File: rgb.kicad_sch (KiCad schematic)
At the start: 55 parts, among them Q1 BSS138, Q2 BSS138, U3 NSI50350ADT4G

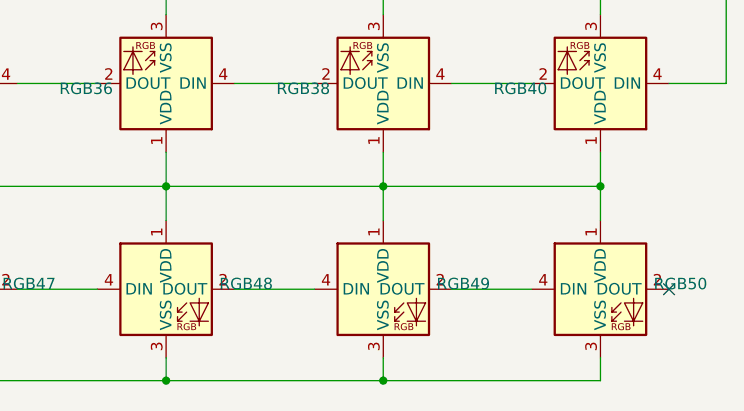
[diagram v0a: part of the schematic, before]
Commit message: finished pcb routing
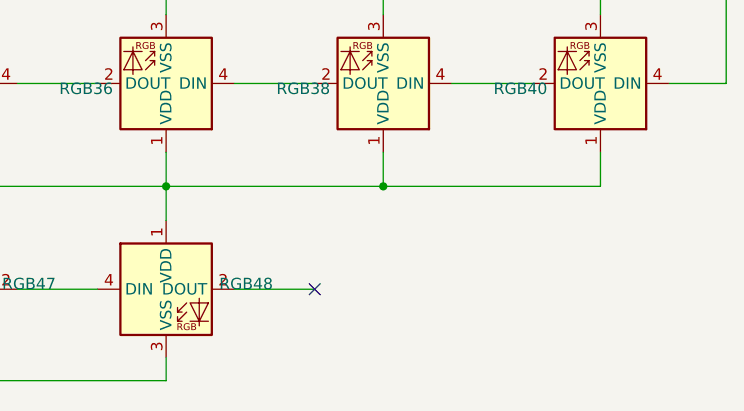
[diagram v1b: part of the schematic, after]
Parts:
- removed RGB49, RGB50: ~, Keebio-Parts.pretty-master:SK6812-MINI-E, symbol New_Library:SK6812_MINI-E_RGB
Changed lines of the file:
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@@
   (junction (at 119.38 81.28) (diameter 0) (color 0 0 0 0)
   )
-  (junction (at 264.16 124.46) (diameter 0) (color 0 0 0 0)
-  )
   (junction (at 167.64 59.69) (diameter 0) (color 0 0 0 0)
   )
@@
   (junction (at 191.77 102.87) (diameter 0) (color 0 0 0 0)
   )
-  (junction (at 240.03 146.05) (diameter 0) (color 0 0 0 0)
-  )
   (junction (at 191.77 38.1) (diameter 0) (color 0 0 0 0)
   )
@@
   (junction (at 71.12 102.87) (diameter 0) (color 0 0 0 0)
   )
-  (junction (at 215.9 146.05) (diameter 0) (color 0 0 0 0)
-  )
-  (no_connect (at 271.78 135.89))
+  (no_connect (at 232.41 135.89))
   (wire (pts (xy 264.16 57.15) (xy 264.16 59.69))
     (stroke (width 0) (type default))
@@
     (stroke (width 0) (type default))
   )
-  (wire (pts (xy 264.16 146.05) (xy 240.03 146.05))
-    (stroke (width 0) (type default))
-  )
   (wire (pts (xy 127 49.53) (xy 135.89 49.53))
     (stroke (width 0) (type default))
@@
     (stroke (width 0) (type default))
   )
-  (wire (pts (xy 247.65 135.89) (xy 256.54 135.89))
-    (stroke (width 0) (type default))
-  )
   (wire (pts (xy 191.77 105.41) (xy 191.77 102.87))
     (stroke (width 0) (type default))
@@
     (stroke (width 0) (type default))
   )
-  (wire (pts (xy 264.16 143.51) (xy 264.16 146.05))
-    (stroke (width 0) (type default))
-  )
   (wire (pts (xy 71.12 62.23) (xy 71.12 59.69))
     (stroke (width 0) (type default))
@@
     (stroke (width 0) (type default))
   )
-  (wire (pts (xy 240.03 143.51) (xy 240.03 146.05))
-    (stroke (width 0) (type default))
-  )
   (wire (pts (xy 240.03 81.28) (xy 264.16 81.28))
     (stroke (width 0) (type default))
@@
     (stroke (width 0) (type default))
   )
-  (wire (pts (xy 264.16 128.27) (xy 264.16 124.46))
-    (stroke (width 0) (type default))
-  )
   (wire (pts (xy 167.64 77.47) (xy 167.64 81.28))
     (stroke (width 0) (type default))
@@
     (stroke (width 0) (type default))
   )
-  (wire (pts (xy 240.03 124.46) (xy 240.03 128.27))
-    (stroke (width 0) (type default))
-  )
   (wire (pts (xy 175.26 69.85) (xy 184.15 69.85))
     (stroke (width 0) (type default))
@@
   )
   (wire (pts (xy 215.9 41.91) (xy 215.9 38.1))
-    (stroke (width 0) (type default))
-  )
-  (wire (pts (xy 215.9 146.05) (xy 240.03 146.05))
     (stroke (width 0) (type default))
   )
@@
     )
   )
-  (symbol (lib_id "New_Library:SK6812_MINI-E_RGB") (at 240.03 135.89 0) (unit 1)
-    (in_bom yes) (on_board yes) (dnp no) (fields_autoplaced)
-    (property "Reference" "RGB49" (at 248.92 135.3059 0)
-      (effects (font (size 1.27 1.27)))
-    )
-    (property "Value" "~" (at 240.03 135.89 0)
-      (effects (font (size 1.27 1.27)))
-    )
-    (property "Footprint" "Keebio-Parts.pretty-master:SK6812-MINI-E" (at 266.7 142.24 0)
-      (effects (font (size 1.27 1.27)) hide)
-    )
-    (property "Datasheet" "" (at 240.03 135.89 0)
-      (effects (font (size 1.27 1.27)) hide)
-    )
-    (pin "1")
-    (pin "2")
-    (pin "3")
-    (pin "4")
-    (instances
-      (project "Keyboard"
-        (path "/2692e4d3-b4ec-4688-a425-bbe94dad9ec3/20b4523f-6bad-4874-b1f4-d51465aeffa0"
-          (reference "RGB49") (unit 1)
-        )
-      )
-    )
-  )
   (symbol (lib_id "New_Library:SK6812_MINI-E_RGB") (at 71.12 113.03 180) (unit 1)
     (in_bom yes) (on_board yes) (dnp no) (fields_autoplaced)
@@
         )
       )
-    )
-  )
-  (symbol (lib_id "New_Library:SK6812_MINI-E_RGB") (at 264.16 135.89 0) (unit 1)
-    (in_bom yes) (on_board yes) (dnp no) (fields_autoplaced)
-    (property "Reference" "RGB50" (at 273.05 135.3059 0)
-      (effects (font (size 1.27 1.27)))
-    )
-    (property "Value" "~" (at 264.16 135.89 0)
-      (effects (font (size 1.27 1.27)))
-    )
-    (property "Footprint" "Keebio-Parts.pretty-master:SK6812-MINI-E" (at 290.83 142.24 0)
-      (effects (font (size 1.27 1.27)) hide)
-    )
-    (property "Datasheet" "" (at 264.16 135.89 0)
-      (effects (font (size 1.27 1.27)) hide)
-    )
-    (pin "1")
-    (pin "2")
-    (pin "3")
-    (pin "4")
-    (instances
-      (project "Keyboard"
-        (path "/2692e4d3-b4ec-4688-a425-bbe94dad9ec3/20b4523f-6bad-4874-b1f4-d51465aeffa0"
-          (reference "RGB50") (unit 1)
-        )
-      )

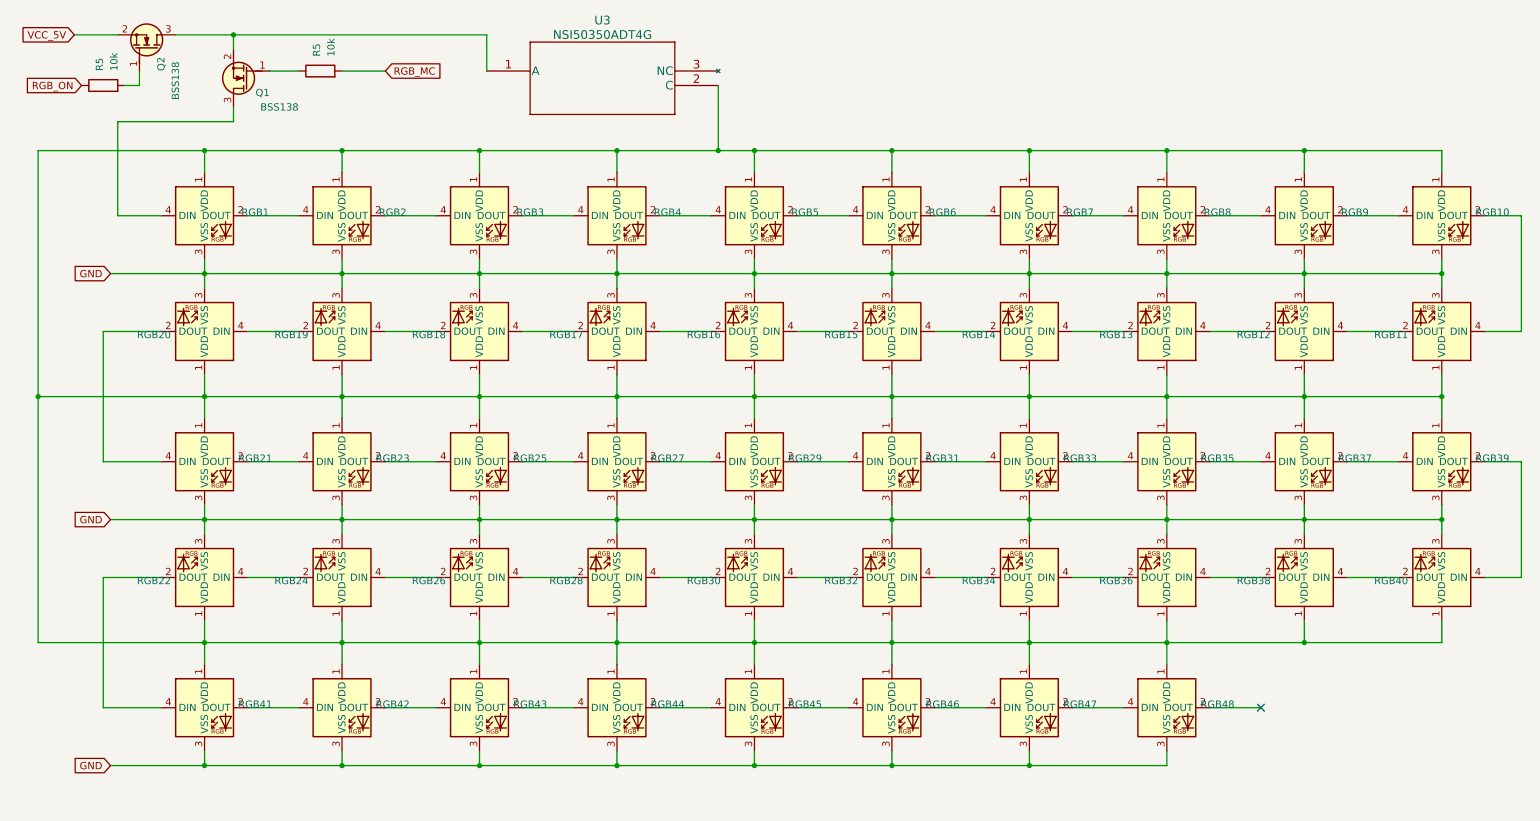
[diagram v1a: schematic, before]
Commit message: changed led mosfet and resistors
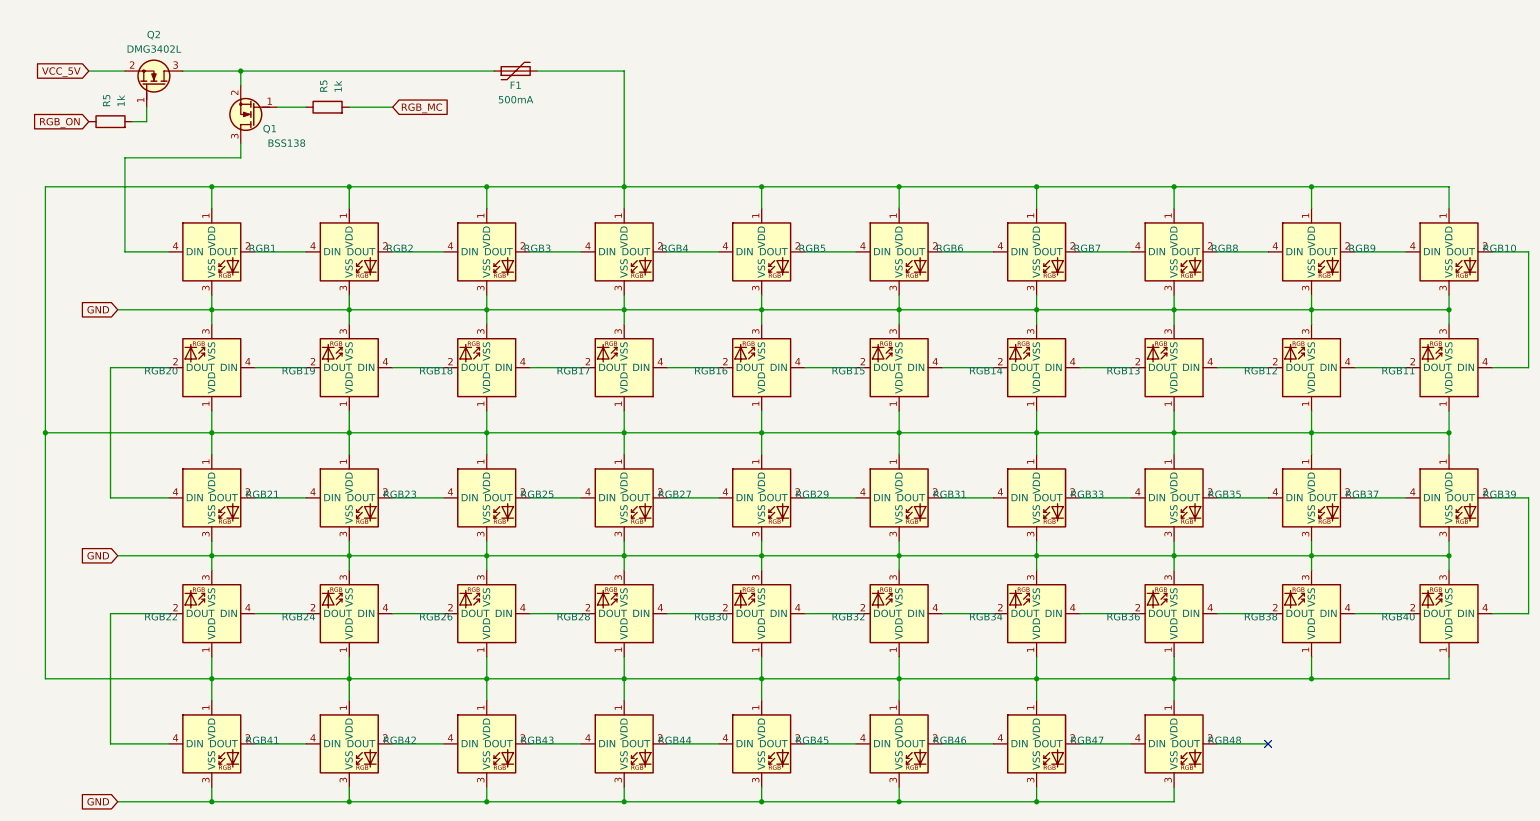
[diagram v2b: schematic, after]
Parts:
- removed Q2: BSS138, PCM_Package_TO_SOT_SMD_AKL:SOT-23, symbol PCM_Transistor_MOSFET_AKL:BSS138
- removed U3: NSI50350ADT4G, footprints:NSI50350ADT4G, symbol 2023-03-04_17-52-59:NSI50350ADT4G
- added F1: 500mA, Fuse:Fuse_1206_3216Metric_Pad1.42x1.75mm_HandSolder, symbol Device:Polyfuse
- added Q2: DMG3402L, PCM_Package_TO_SOT_SMD_AKL:SOT-23, symbol PCM_Transistor_MOSFET_AKL:DMG3402L
- R5: value 10k -> 1k
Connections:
- net VCC_5V: now also Q2.2 (S)
- net at RGB1.1 (VDD), RGB10.1 (VDD), RGB11.1 (VDD)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: now also F1.2
- net at Q1.2 (S): now also F1.1, Q2.3 (D)
- net at R5.2: now also Q2.1 (G)
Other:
- company: (none) -> 0xAC0
- title: (none) -> Keyboard RGB LEDs
- moved on the sheet: Q1, R5, RGB1, RGB10, RGB11, RGB12, RGB13, RGB14, RGB15, RGB16, RGB17, RGB18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
